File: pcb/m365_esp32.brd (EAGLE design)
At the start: 23 x 72 mm, 71 parts, among them J2 105133-0011, Q1 32768kHz, T1 L2N7002DW1T1G, T2 L2N7002DW1T1G

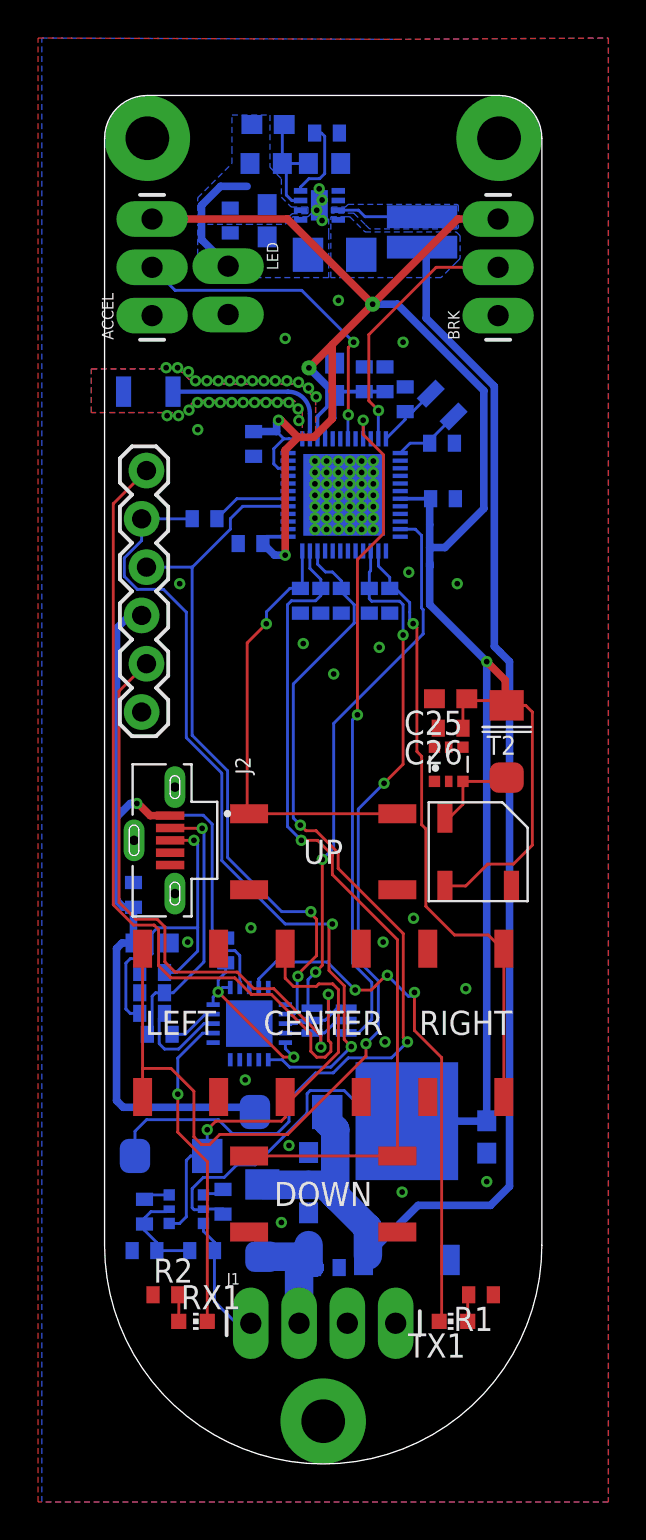
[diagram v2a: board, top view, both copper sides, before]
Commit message: Finished dashboard PCB
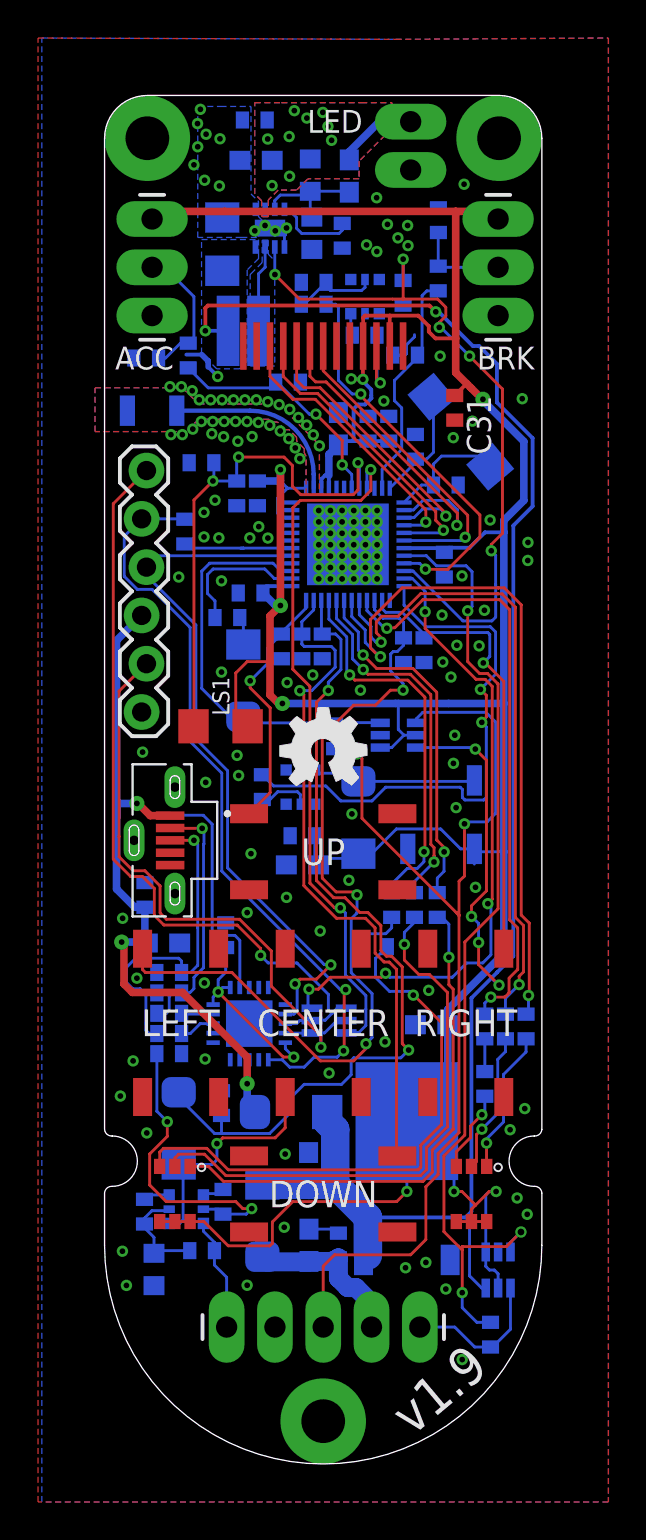
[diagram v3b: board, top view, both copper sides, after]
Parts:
- removed Q1: 32768kHz, crystal:FC-12M
- removed RX1, TX1: (no value), adafruit:CHIP-LED0603
- added C28, C29, C30, C31: 0.1uF, eagle-ltspice:C0402
- added D5: SMAFJ75A, my-lib:SMAFJ75A
- added FT231X: FT231XQ-R, FT231XQ-R:FT231XQ-R
- added GOLD_ORB_SM2: OSHWLOGOLOGO5MM, oshw:OSHW_5MM
- added IC1, IC2: NTS0101GW,125, NTS0101GW_125:SOT65P210X110-6N
- added LS1: (no value), eagle-ltspice:R1206
- added M365_CONNECTOR: (no value), SparkFun-Connectors:1X05_LONGPADS
- added R13: 16R, eagle-ltspice:R0402
- added R14, R24, R25, R28, R29, R31: 866k, eagle-ltspice:R0402
- added R15, R30, R32: 220R, eagle-ltspice:R0402
- added R17, R20, R23: 86.6R, eagle-ltspice:R0402
- added R18, R21: 60.4R, eagle-ltspice:R0402
- added R19, R22, R26, R27: 37.4R, eagle-ltspice:R0402
- added REG: UZ1085L-33-TN3-R, my-lib:TO-252-2
- added T3: L2N7002DW1T1G, nxp_60_1_1:SOT363
- added U$10: X321532768KGB2SI, my-lib:SMD-3215_2P
- added U$11: LH096T-IG11, my-lib:LH096T-IG11
- added USB: 105133-0011, 105133-0011:MOLEX_105133-0011
- C1: value 10u -> 10uF
- C10, C15, C22, C25, C7, C8: value 22u -> 22uF
- C23, C24: value 15pF -> 20pF
- C6: value 100p -> 100pF
- J1: device SparkFun-Connectors:1X04_LONGPADS -> eagle-ltspice:R0402
- J2: value 105133-0011 -> (none); device 105133-0011:MOLEX_105133-0011 -> eagle-ltspice:R0402
- R1, R2: value 499 -> 499R; device resistor:R0402 -> eagle-ltspice:R0402
- R11: device eagle-ltspice:R0402 -> eagle-ltspice:R0603
- R3, R4: value 27 -> 27R
- U$2: value FT231XQ-R -> Z3535RGBA; device FT231XQ-R:FT231XQ-R -> my-lib:Z3535RGBA
- U$7: value UZ1085L-33-TN3-R -> Z3535RGBA; device my-lib:TO-252-2 -> my-lib:Z3535RGBA
- moved R1 53.5 mm to (6.05, 62.4), flipped to the bottom, turned to 270 degrees
- moved R2 49.4 mm to (-7.10, 58.3), flipped to the bottom, turned to 270 degrees
- moved U$2 14.7 mm to (7.80, 14.2), flipped to the top
- moved J1 12.6 mm to (8.80, 6.80), flipped to the bottom, turned to 90 degrees
- moved U$7 12.5 mm to (-7.80, 14.2), flipped to the top, turned to 90 degrees
- moved LED 12.2 mm to (4.60, 70.6)
- moved C25 11.7 mm to (-1.09, 31.5), flipped to the bottom, turned to 0 degrees
- moved L1 10.7 mm to (-4.20, 59.6), turned to 270 degrees
- moved J2 10.0 mm to (0.60, 38.3), flipped to the bottom, turned to 90 degrees
- moved C26 9.63 mm to (-1.09, 33.0), flipped to the bottom, turned to 0 degrees
- moved D2 8.77 mm to (1.85, 34.0), flipped to the bottom, turned to 270 degrees
- moved T2 7.89 mm to (-1.20, 35.6), flipped to the bottom, turned to 180 degrees
- moved C8 6.57 mm to (5.70, 23.1), turned to 0 degrees
- moved C1 5.94 mm to (-5.31, 64.2), turned to 270 degrees
- moved R5 5.46 mm to (1.00, 64.6), turned to 90 degrees
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- renumbered ACCEL to ACC, J3 to PROG
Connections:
- removed net A3: U$1.8
- removed net A4: U$1.10
- removed net CBUS3: RX1.C, U$2.P$7
- removed net CBUS4: TX1.C, U$2.P$14
- removed net D10: U$1.21
- removed net D8: U$1.17
- removed net D9: U$1.20
- removed net DATA: J1.3
- new net !TFTRST: U$1.14, U$11.P$6
- new net BACKLIGHT: R15.1, U$1.21
- new net BTN_CONTROL: R30.1
- new net DC: U$1.15, U$11.P$5
- new net LED_K: R13.2, U$11.P$11
- new net LIGHT_SENS: C30.1, LS1.2, R28.2, U$1.8
- new net LL_B: R21.1, U$1.31
- new net LL_G: R22.1, U$1.32
- new net LL_R: R23.1, U$1.33
- new net LR_B: R18.1, U$1.30
- new net LR_G: R19.1, U$1.29
- new net LR_R: R20.1, U$1.28
- new net M365_DATA: IC2.4, J2.1, M365_CONNECTOR.3
- new net M365_DATA_3V3: D5.P$2, IC2.3, J2.2, U$1.39
- new net M365_LED_DATA: IC1.4, J1.1, M365_CONNECTOR.1
- new net M365_LED_DATA_3V3: IC1.3, J1.2, U$1.20
- new net MOSI: U$1.16, U$11.P$3
- new net N$13: R13.1, T3.6
- new net N$14: R14.2, R15.2, T3.2
- new net N$15: D5.P$1, R17.2
- new net N$16: C29.2, R2.2, U$1.7
- new net N$17: R17.1, U$1.38
- new net N$18: R21.2, U$7.B
- new net N$19: R22.2, U$7.G
- new net N$20: R26.2, U$7.R
- new net N$21: R18.2, U$2.B
- new net N$22: R19.2, U$2.G
- new net N$23: U$1.43
- new net N$25: R27.2, U$2.R
- new net N$26: R20.2, R27.1
- new net N$27: U$1.40
- new net N$28: R10.2, R30.2, T1.2
- new net N$29: R32.2, T2.5
- new net SCK: U$1.17, U$11.P$4
- new net TFTCS: U$1.18, U$11.P$7
- net !DTR1: now also FT231X.P$18; no longer U$2.P$18
- net !RTS1: now also FT231X.P$19; no longer U$2.P$19
- net 32K_XP: now also U$10.P$2; no longer Q1.2
- net 3V3: now also C31.1, IC1.1, IC1.5, IC2.1, IC2.5, LS1.1, REG.3, U$11.P$10, U$11.P$12, U$2.ANODE_$1, U$2.ANODE_$2, U$2.ANODE_$3, U$7.ANODE_$1, U$7.ANODE_$2, U$7.ANODE_$3; no longer R10.2, T1.2, U$7.3
- net 42V: now also M365_CONNECTOR.5; no longer J1.1
- net 5V: now also IC1.6, IC2.6, REG.2; no longer U$7.2
- net 5V_IN: now also M365_CONNECTOR.2; no longer J1.2
- net 5V_USB: now also FT231X.P$12, USB.1; no longer J2.1, R1.1, R2.1, U$2.P$12
- net A2: now also R2.1, R25.1; no longer U$1.7
- net A5: now also R1.1, R24.2; no longer U$1.11
- net BTN_CENTER: now also R31.1
- net BUZZER: now also R32.1, U$1.24; no longer T2.5
- net GND: now also C28.1, C29.1, C30.2, C31.2, FT231X.P$13, FT231X.P$21, FT231X.P$3, IC1.2, IC2.2, M365_CONNECTOR.4, R14.1, R24.1, R25.2, R28.1, R29.1, R31.2, REG.1, T3.1, U$11.P$13, U$11.P$8, USB.5, USB.S1, USB.S2, USB.S3; no longer J1.4, J2.5, J2.S1, J2.S2, J2.S3, U$2.P$13, U$2.P$21, U$2.P$3, U$7.1
- net LED_EN: now also R29.2, U$1.22
- net N$2: now also U$10.P$1; no longer Q1.1
- net N$3: now also R23.2, R26.1; no longer R1.2, TX1.A
- net N$4: now also C28.2, R1.2, U$1.11; no longer R2.2, RX1.A
- net N$6: now also FT231X.P$10, FT231X.P$11, FT231X.P$20; no longer U$2.P$10, U$2.P$11, U$2.P$20
- net RX0: now also FT231X.P$17; no longer U$2.P$17
- net TX0: now also FT231X.P$1; no longer U$2.P$1
- net USB-DATA_M: now also USB.2; no longer J2.2
- net USB-DATA_P: now also USB.3; no longer J2.3
- net USBDM: now also FT231X.P$9; no longer U$2.P$9
- net USBDP: now also FT231X.P$8; no longer U$2.P$8
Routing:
- net M365_DATA: track 0.00 -> 55.5 mm, vias 0 -> 2
- net M365_LED_DATA_3V3: track 0.00 -> 51.9 mm, vias 0 -> 3
- net 3V3: track 155.0 -> 196.2 mm, vias 5 -> 9
- net LED_EN: track 0.00 -> 38.9 mm, vias 0 -> 5
- net LR_B: track 0.00 -> 36.6 mm, vias 0 -> 2
- net LR_G: track 0.00 -> 34.2 mm, vias 0 -> 2
- net 5V: track 73.4 -> 105.5 mm, vias 0 -> 6
- net LR_R: track 0.00 -> 31.9 mm, vias 0 -> 2
- net N$19: track 0.00 -> 29.6 mm, vias 0 -> 1
- net N$20: track 0.00 -> 29.5 mm, vias 0 -> 1
- net BUZZER: track 0.00 -> 29.0 mm, vias 0 -> 2
- net CBUS4: track 28.5 -> 0.00 mm, vias 3 -> 0
- net N$18: track 0.00 -> 27.6 mm, vias 0 -> 1
- net LIGHT_SENS: track 0.00 -> 27.5 mm, vias 0 -> 3
- net M365_DATA_3V3: track 0.00 -> 21.4 mm
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- added copper zone on layer 1, net FRONT_LED
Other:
- outline, holes or cut-outs redrawn
- board text added: "JLCJLCJLCJLC"
- board text added: "v1.9"

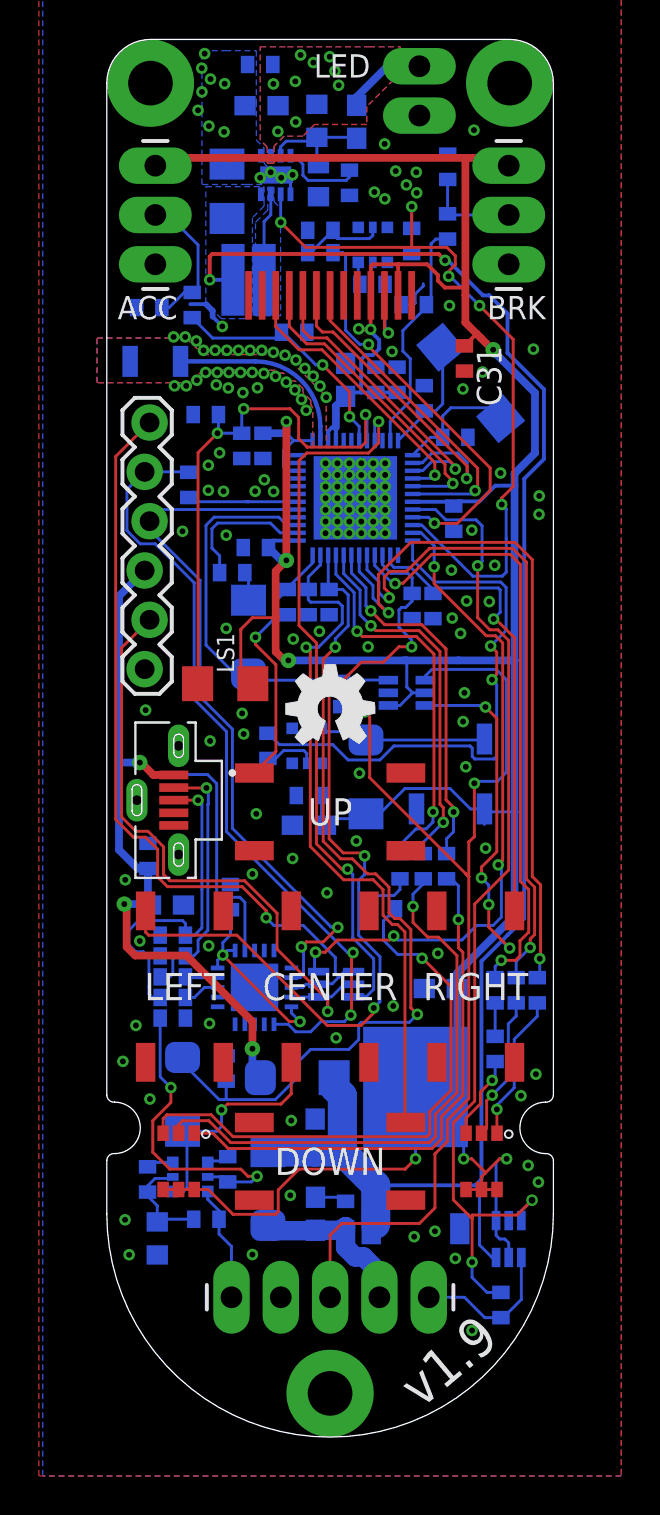
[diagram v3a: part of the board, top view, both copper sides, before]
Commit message: Updated dashboard PCB design. Replaced ESP32-D0DW with ESP32-PicoD4 Added bigger buzzer footprint Removed RGB led
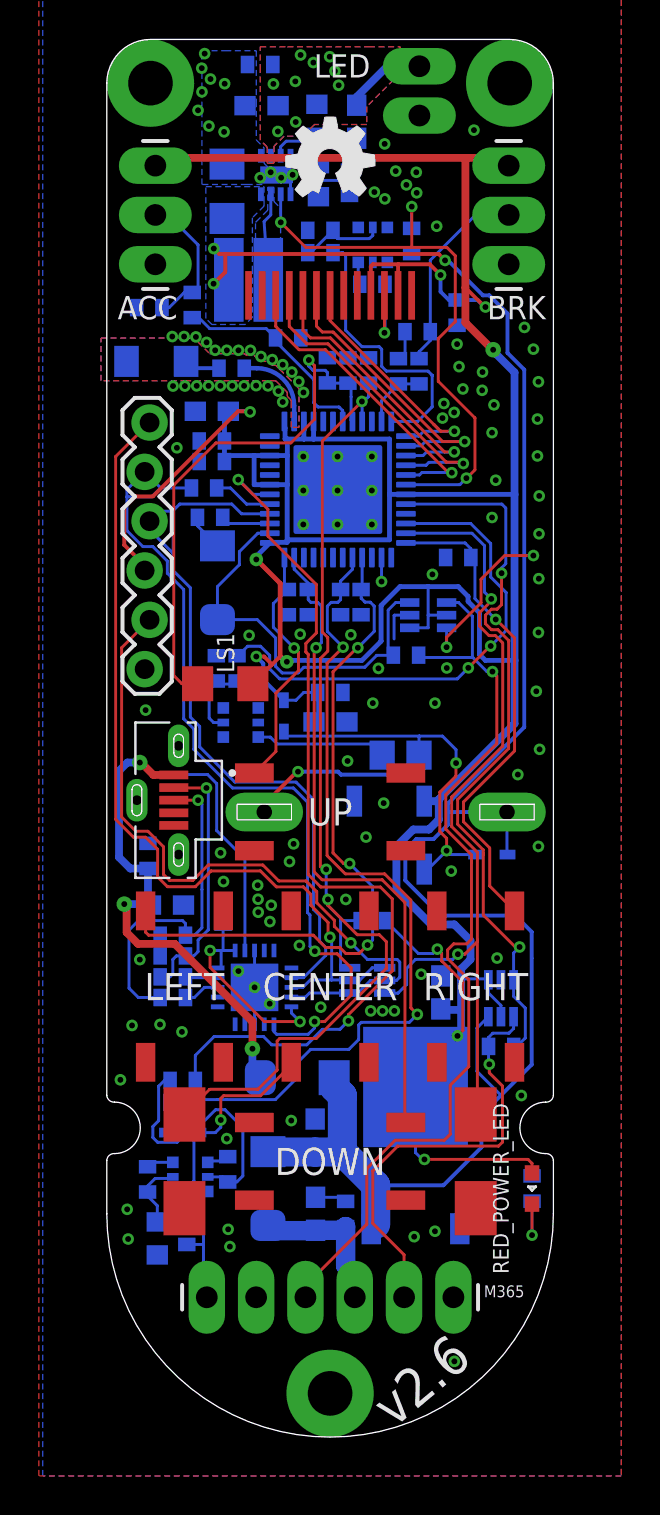
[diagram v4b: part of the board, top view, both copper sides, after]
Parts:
- removed C20: 0.1uF, eagle-ltspice:C0402
- removed C23, C24: 20pF, resistor:C0402
- removed D2: SMAFJ75A, my-lib:SMAFJ75A
- removed M365_CONNECTOR: (no value), SparkFun-Connectors:1X05_LONGPADS
- removed R22, R26, R27: 37.4R, eagle-ltspice:R0402
- removed R23: 86.6R, eagle-ltspice:R0402
- removed U$10: X321532768KGB2SI, my-lib:SMD-3215_2P
- removed U$7: Z3535RGBA, my-lib:Z3535RGBA
- added D6, D7: BAS516,115, BAS516_115:SOD1608X65N
- added IC3: UNEXPECTEDMAKER_ESP32-PICO-D4, m365_esp32:UNEXPECTEDMAKER_PICO-D4-QFN48
- added M365: (no value), SparkFun-Connectors:1X06_LONGPADS
- added RED_POWER_LED: (no value), Wurth_Elektronik_Optoelectronics_rev18a:WL-SMCD_0603
- added U$6: ZL-YDW2722-2705PF-12.5ZL-YDW2722-2705PF-12.5, my-lib:ZL-YDW2722-2705PF-12.5
- C19: value 0.1uF -> (none)
- D1: value SMAFJ75A -> BAS516,115; device my-lib:SMAFJ75A -> BAS516_115:SOD1608X65N
- R18: value 60.4R -> 300R
- R19: value 37.4R -> 866k
- R20: value 86.6R -> 866k
- R21: value 60.4R -> ??; device eagle-ltspice:R0402 -> eagle-ltspice:R0805
- R6: value 715k -> 787k
- U$1: value ESP32 -> TL3302BF260QJ; device esp32:QFN48-0.4MM -> my-lib:TL3302BF260QJ
- U$2: value Z3535RGBA -> TL3302BF260QJ; device my-lib:Z3535RGBA -> my-lib:TL3302BF260QJ
- moved U$1 34.7 mm to (7.50, 14.2), flipped to the top
- moved GOLD_ORB_SM2 28.2 mm to (0.00, 65.7)
- moved R20 21.9 mm to (-5.86, 39.6)
- moved D1 20.2 mm to (8.33, 30.0), turned to 0 degrees
- moved U$2 15.3 mm to (-7.50, 14.2), turned to 270 degrees
- moved C19 13.8 mm to (-5.07, 55.0), turned to 180 degrees
- moved J1 13.3 mm to (8.81, 20.1), turned to 180 degrees
- moved IC1 12.4 mm to (8.80, 22.6)
- moved C18 10.8 mm to (1.98, 54.9), turned to 90 degrees
- moved C16 10.4 mm to (-6.09, 50.2), turned to 0 degrees
- moved R18 10.2 mm to (10.4, 12.8)
- moved C17 9.02 mm to (-6.09, 51.3), turned to 0 degrees
- moved R24 8.63 mm to (4.51, 56.9), turned to 180 degrees
- moved R19 8.21 mm to (2.20, 26.6), turned to 0 degrees
- moved R1 7.60 mm to (4.58, 54.9)
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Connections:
- removed net 32K_XP: C23.1, U$1.12, U$10.P$2
- removed net LIGHT_SENS: C30.1, LS1.2, R28.2, U$1.8
- removed net LL_B: R21.1, U$1.31
- removed net LL_G: R22.1, U$1.32
- removed net LL_R: R23.1, U$1.33
- removed net LR_B: R18.1, U$1.30
- removed net LR_G: R19.1, U$1.29
- removed net LR_R: R20.1, U$1.28
- removed net N$16: C29.2, R2.2, U$1.7
- removed net N$18: R21.2, U$7.B
- removed net N$19: R22.2, U$7.G
- removed net N$20: R26.2, U$7.R
- removed net N$21: R18.2, U$2.B
- removed net N$22: R19.2, U$2.G
- removed net N$23: U$1.43
- removed net N$25: R27.2, U$2.R
- removed net N$26: R20.2, R27.1
- removed net N$27: U$1.40
- removed net RESET: U$1.9, UMH3N1.6
- new net ENABLE: C18.1, IC3.9, R19.2, U$2.P$1, UMH3N1.3
- new net GPIO15_NOT_USED: IC3.21
- new net GPIO35: C28.2, IC3.11, R1.2
- new net GPIO38: C29.2, IC3.7, R2.2
- new net INTERNAL_FLASH_CLK: IC3.31
- new net INTERNAL_FLASH_CMD: IC3.30
- new net INTERNAL_FLASH_GPIO16: IC3.25
- new net INTERNAL_FLASH_GPIO17: IC3.27
- new net INTERNAL_FLASH_SD0: IC3.32
- new net INTERNAL_FLASH_SD1: IC3.33
- new net SENSOR_VN: C30.1, IC3.8, LS1.2, R28.2
- new net VDD_SDIO: IC3.26
- net !TFTRST: now also IC3.14; no longer U$1.14
- net 3V3: now also D6.1, IC3.1, IC3.19, IC3.3, IC3.37, IC3.4, IC3.43, IC3.46, PROG.3, R19.1, RED_POWER_LED.2; no longer C18.1, C19.1, C20.1, D2.P$1, U$1.1, U$1.19, U$1.3, U$1.37, U$1.4, U$1.46, U$2.ANODE_$1, U$2.ANODE_$2, U$2.ANODE_$3, U$7.ANODE_$1, U$7.ANODE_$2, U$7.ANODE_$3
- net 42V: now also M365.6; no longer M365_CONNECTOR.5
- net 5V: now also D1.1, U$6.P$1
- net 5V_IN: now also M365.3; no longer M365_CONNECTOR.2
- net 5V_USB: no longer PROG.3
- net BACKLIGHT: now also IC3.12; no longer U$1.21
- net BTN_CENTER: now also D7.2, IC3.29; no longer D1.P$2, U$1.34
- net BTN_CONTROL: now also IC3.42
- net BTN_DOWN: now also IC3.35; no longer U$1.35
- net BTN_LEFT: now also IC3.28; no longer U$1.27
- net BTN_RIGHT: now also IC3.24; no longer U$1.26
- net BTN_UP: now also IC3.36; no longer U$1.36
- net BUZZER: now also IC3.22; no longer U$1.24
- net DC: now also IC3.15; no longer U$1.15
- net GND: now also IC3.EXP, M365.5, R18.1, R20.1, U$1.P$2, U$2.P$2; no longer C19.2, C20.2, C23.2, C24.2, M365_CONNECTOR.4, U$1.EP
- net GPIO0: now also IC3.23, U$1.P$1, UMH3N1.6; no longer U$1.23, UMH3N1.3
- net LED_EN: now also IC3.18; no longer U$1.22
- net LNA_IN: now also C19.2, IC3.2; no longer ANT1.1, U$1.2
- net M365_DATA: now also M365.4; no longer M365_CONNECTOR.3
- net M365_DATA_3V3: now also IC3.38; no longer U$1.39
- net M365_LED_DATA: now also M365.2; no longer M365_CONNECTOR.1
- net M365_LED_DATA_3V3: now also IC3.20; no longer U$1.20
- net MOSI: now also IC3.17; no longer U$1.16
- net N$1: now also IC3.41; no longer U$1.42
- net N$11: now also D1.2, D6.2, R21.2, U$6.P$2, U$8.P$3; no longer CENTER.P$1, CENTER.P$4, D1.P$1, T1.4
- net N$12: now also R21.1; no longer D2.P$2, U$8.P$1
- net N$17: now also IC3.39; no longer U$1.38
- net N$2: now also ANT1.1, C19.1; no longer C24.1, U$1.13, U$10.P$1
- net N$29: now also R20.2
- net N$3: now also R18.2, RED_POWER_LED.1; no longer R23.2, R26.1
- net N$4: now also CENTER.P$1, CENTER.P$4, D7.1, T1.4; no longer C28.2, R1.2, U$1.11
- net RX0: now also IC3.40; no longer U$1.41
- net SCK: now also IC3.16; no longer U$1.17
- net TFTCS: now also IC3.13; no longer U$1.18
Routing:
- net ENABLE: track 0.00 -> 54.3 mm, vias 0 -> 3
- net BTN_CONTROL: track 0.00 -> 46.6 mm, vias 0 -> 2
- net RESET: track 36.9 -> 0.00 mm, vias 2 -> 0
- net LR_B: track 36.6 -> 0.00 mm, vias 2 -> 0
- net LR_G: track 34.2 -> 0.00 mm, vias 2 -> 0
- net LR_R: track 31.9 -> 0.00 mm, vias 2 -> 0
- net N$19: track 29.6 -> 0.00 mm, vias 1 -> 0
- net N$20: track 29.5 -> 0.00 mm, vias 1 -> 0
- net SENSOR_VN: track 0.00 -> 28.6 mm, vias 0 -> 1
- net N$18: track 27.6 -> 0.00 mm, vias 1 -> 0
- net LIGHT_SENS: track 27.5 -> 0.00 mm, vias 3 -> 0
- net LL_R: track 20.1 -> 0.00 mm, vias 2 -> 0
- net 3V3: track 196.2 -> 216.0 mm, vias 9 -> 10
- net LL_G: track 19.2 -> 0.00 mm, vias 2 -> 0
- net LL_B: track 18.8 -> 0.00 mm, vias 2 -> 0
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- added copper zone on layer 1, net NC
- added copper zone on layer 16, net NC1
- removed copper zone on layer 16, net NO_GND1
- removed copper zone on layer 1, net NO_GND2
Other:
- board text added: "42V"
- board text added: "5V"
- board text added: "DATA"
- board text added: "GND"
- board text added: "NC"
- board text added: "RGB"
- board text added: "v2.6"
- board text removed: "v1.9"
